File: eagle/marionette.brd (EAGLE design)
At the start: 112.4 x 152.7 mm, 47 parts, among them J2 SWD_CONNECTOR, J3 2X10FE, J4 2X10FE, J5 2X10FE, J6 2X10FE, J7 2X10FE, U1 USB3318, U2 NCP705, U3 XCL206B, X1 ABS25-32.768KHZ-6-T

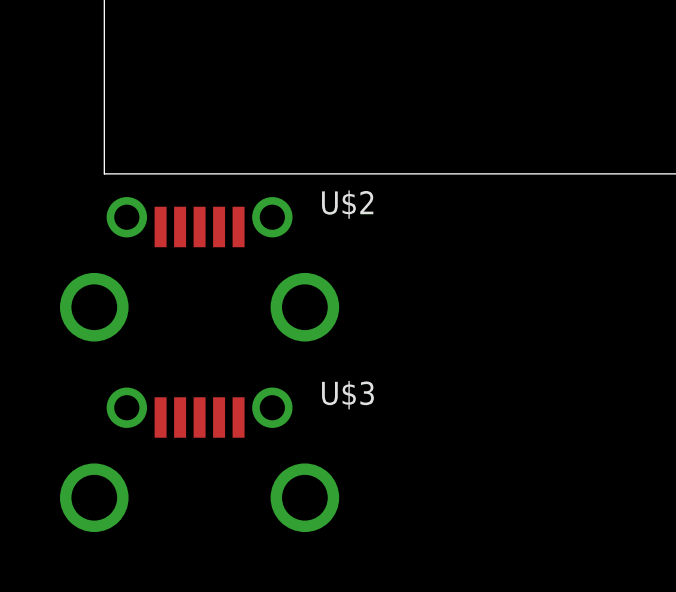
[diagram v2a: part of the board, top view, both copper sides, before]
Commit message: Replaced resistors and capacitors with Marionette library components
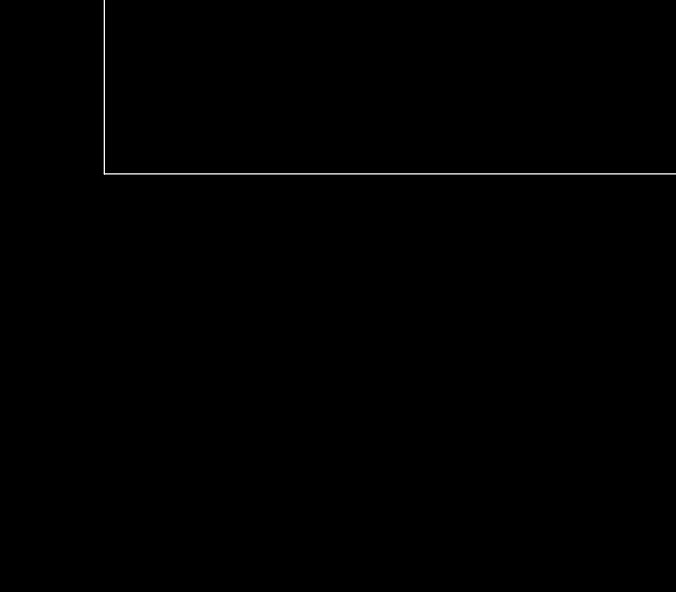
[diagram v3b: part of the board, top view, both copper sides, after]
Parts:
- removed U$2, U$3: ZX62D-B-5P8, con-hirose-microusb:ZX62D-B-5P8
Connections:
- removed net FS_DM: U$1.122, U$2.P2
- removed net FS_DP: U$1.123, U$2.P3
- removed net FS_ID: U$1.121, U$2.P4
- removed net OTG_VBUS: D2.P$1, U$1.120, U$2.P1
- removed net SHLD: U$3.P$1, U$3.P$2, U$3.P$3, U$3.P$4
- removed net VCC: U$3.P1
- new net N$13: U$1.122
- new net N$14: U$1.123
- new net N$2: U$1.120
- new net N$6: U$1.121
- net GND: no longer U$2.P$1, U$2.P$2, U$2.P$3, U$2.P$4, U$2.P5
- net N$12: no longer U$3.P5
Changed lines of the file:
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@@
 <layer number="54" name="bGND_GNDA" color="1" fill="9" visible="no" active="no"/>
 <layer number="56" name="wert" color="7" fill="1" visible="no" active="no"/>
-<layer number="59" name="Invisible" color="7" fill="1" visible="yes" active="yes"/>
-<layer number="61" name="stand" color="7" fill="1" visible="yes" active="yes"/>
 <layer number="90" name="Modules" color="5" fill="1" visible="no" active="no"/>
 <layer number="91" name="Nets" color="2" fill="1" visible="no" active="no"/>
@@
 <layer number="107" name="Crop" color="7" fill="1" visible="no" active="yes"/>
 <layer number="108" name="dxf_notes" color="14" fill="1" visible="yes" active="yes"/>
-<layer number="109" name="fp9" color="7" fill="1" visible="yes" active="yes"/>
 <layer number="110" name="labels" color="7" fill="1" visible="yes" active="yes"/>
 <layer number="111" name="print" color="7" fill="1" visible="yes" active="yes"/>
@@
 <layer number="121" name="_tsilk" color="7" fill="1" visible="no" active="yes"/>
 <layer number="122" name="_bsilk" color="7" fill="1" visible="no" active="yes"/>
-<layer number="123" name="tTestmark" color="7" fill="1" visible="yes" active="yes"/>
-<layer number="124" name="bTestmark" color="7" fill="1" visible="yes" active="yes"/>
 <layer number="125" name="_tNames" color="7" fill="1" visible="no" active="yes"/>
-<layer number="126" name="_bNames" color="7" fill="1" visible="yes" active="yes"/>
-<layer number="127" name="_tValues" color="7" fill="1" visible="yes" active="yes"/>
-<layer number="128" name="_bValues" color="7" fill="1" visible="yes" active="yes"/>
-<layer number="130" name="bLogo" color="7" fill="1" visible="yes" active="yes"/>
-<layer number="131" name="tText" color="7" fill="1" visible="yes" active="yes"/>
-<layer number="132" name="bMask" color="7" fill="1" visible="yes" active="yes"/>
 <layer number="144" name="Drill_legend" color="7" fill="1" visible="no" active="yes"/>
 <layer number="151" name="HeatSink" color="7" fill="1" visible="no" active="yes"/>
-<layer number="152" name="_bDocu" color="7" fill="1" visible="yes" active="yes"/>
-<layer number="199" name="Contour" color="7" fill="1" visible="yes" active="yes"/>
 <layer number="200" name="200bmp" color="1" fill="10" visible="no" active="yes"/>
 <layer number="201" name="201bmp" color="2" fill="10" visible="no" active="yes"/>
@@
 <layer number="223" name="223bmp" color="24" fill="1" visible="no" active="no"/>
 <layer number="224" name="224bmp" color="25" fill="1" visible="no" active="no"/>
-<layer number="225" name="225bmp" color="7" fill="1" visible="yes" active="yes"/>
-<layer number="226" name="226bmp" color="7" fill="1" visible="yes" active="yes"/>
-<layer number="227" name="227bmp" color="7" fill="1" visible="yes" active="yes"/>
-<layer number="228" name="228bmp" color="7" fill="1" visible="yes" active="yes"/>
-<layer number="231" name="Eagle3D_PG1" color="7" fill="1" visible="yes" active="yes"/>
-<layer number="232" name="Eagle3D_PG2" color="7" fill="1" visible="yes" active="yes"/>
-<layer number="233" name="Eagle3D_PG3" color="7" fill="1" visible="yes" active="yes"/>
-<layer number="248" name="Housing" color="7" fill="1" visible="yes" active="yes"/>
-<layer number="249" name="Edge" color="7" fill="1" visible="yes" active="yes"/>
 <layer number="250" name="Descript" color="3" fill="1" visible="no" active="no"/>
 <layer number="251" name="SMDround" color="12" fill="11" visible="no" active="no"/>
@@
 <element name="J6" library="20POS_ANGLED_FEMALE_HEADER" package="2X10_FEMALE_ANGLED" value="2X10FE" x="76.2" y="14.605"/>
 <element name="J7" library="20POS_ANGLED_FEMALE_HEADER" package="2X10_FEMALE_ANGLED" value="2X10FE" x="41.91" y="14.605"/>
-<element name="U$2" library="con-hirose-microusb" package="ZX62D-B-5P8" value="ZX62D-B-5P8" x="3.175" y="-4.445"/>
-<element name="U$3" library="con-hirose-microusb" package="ZX62D-B-5P8" value="ZX62D-B-5P8" x="3.175" y="-10.795"/>
 </elements>
 <signals>
@@
 <contactref element="C28" pad="2"/>
 <contactref element="C29" pad="2"/>
-<contactref element="U$3" pad="P5"/>
 <wire x1="35.56" y1="35.14" x2="38.1" y2="35.14" width="0" layer="19" extent="1-1"/>
 <wire x1="33.02" y1="35.14" x2="35.56" y2="35.14" width="0" layer="19" extent="1-1"/>
 <wire x1="36.83" y1="29.21" x2="38.1" y2="35.14" width="0" layer="19" extent="1-1"/>
-<wire x1="4.475" y1="-8.12" x2="36.83" y2="29.21" width="0" layer="19" extent="1-1"/>
 </signal>
 <signal name="N$7">
@@
 <contactref element="J4" pad="20"/>
 <contactref element="J3" pad="20"/>
-<contactref element="U$2" pad="P5"/>
-<contactref element="U$2" pad="P$1"/>
-<contactref element="U$2" pad="P$2"/>
-<contactref element="U$2" pad="P$3"/>
-<contactref element="U$2" pad="P$4"/>
 <wire x1="101.6" y1="64.135" x2="101.6" y2="95.885" width="0" layer="19" extent="1-1"/>
 <wire x1="78.955" y1="60.96" x2="101.6" y2="64.135" width="0" layer="19" extent="1-1"/>
@@
 <wire x1="101.6" y1="33.02" x2="78.955" y2="43.815" width="0" layer="19" extent="1-1"/>
 <wire x1="87.63" y1="13.335" x2="101.6" y2="33.02" width="0" layer="19" extent="1-1"/>
-<wire x1="5.6" y1="-1.445" x2="19.9" y2="44.45" width="0" layer="19" extent="1-1"/>
-<wire x1="4.475" y1="-1.77" x2="5.6" y2="-1.445" width="0" layer="19" extent="1-1"/>
-<wire x1="6.685" y1="-4.445" x2="5.6" y2="-1.445" width="0" layer="19" extent="1-1"/>
-<wire x1="0.75" y1="-1.445" x2="4.475" y2="-1.77" width="0" layer="19" extent="1-1"/>
-<wire x1="-0.335" y1="-4.445" x2="0.75" y2="-1.445" width="0" layer="19" extent="1-1"/>
 </signal>
 <signal name="SDIO_D4">
@@
 <contactref element="U$1" pad="58"/>
 </signal>
+<signal name="N$2">
+<contactref element="U$1" pad="120"/>
+</signal>
+<signal name="N$6">
+<contactref element="U$1" pad="121"/>
+</signal>
+<signal name="N$13">
+<contactref element="U$1" pad="122"/>
+</signal>
+<signal name="N$14">
+<contactref element="U$1" pad="123"/>
+</signal>
 <signal name="PA15">
 <contactref element="U$1" pad="138"/>
@@
 <wire x1="18.2" y1="44.45" x2="18.39" y2="46.065" width="0" layer="19" extent="1-1"/>
 </signal>
-<signal name="SHLD">
-<contactref element="U$3" pad="P$1"/>
-<contactref element="U$3" pad="P$2"/>
-<contactref element="U$3" pad="P$3"/>
-<contactref element="U$3" pad="P$4"/>
-<wire x1="0.75" y1="-7.795" x2="-0.335" y2="-10.795" width="0" layer="19" extent="1-1"/>
-<wire x1="5.6" y1="-7.795" x2="0.75" y2="-7.795" width="0" layer="19" extent="1-1"/>
-<wire x1="6.685" y1="-10.795" x2="5.6" y2="-7.795" width="0" layer="19" extent="1-1"/>
-</signal>
-<signal name="VCC">
-<contactref element="U$3" pad="P1"/>
-</signal>
-<signal name="OTG_VBUS">
-<contactref element="U$1" pad="120"/>
-<contactref element="U$2" pad="P1"/>
-<contactref element="D2" pad="P$1"/>
-<wire x1="13.12" y1="53.34" x2="73.71" y2="58.09" width="0" layer="19" extent="1-1"/>
-<wire x1="1.875" y1="-1.77" x2="13.12" y2="53.34" width="0" layer="19" extent="1-1"/>
-</signal>
-<signal name="FS_ID">
-<contactref element="U$1" pad="121"/>
-<contactref element="U$2" pad="P4"/>
-<wire x1="3.825" y1="-1.77" x2="73.71" y2="58.59" width="0" layer="19" extent="1-1"/>
-</signal>
-<signal name="FS_DM">
-<contactref element="U$1" pad="122"/>
-<contactref element="U$2" pad="P2"/>
-<wire x1="2.525" y1="-1.77" x2="73.71" y2="59.09" width="0" layer="19" extent="1-1"/>
-</signal>
-<signal name="FS_DP">
-<contactref element="U$1" pad="123"/>
-<contactref element="U$2" pad="P3"/>
-<wire x1="3.175" y1="-1.77" x2="73.71" y2="59.59" width="0" layer="19" extent="1-1"/>
-</signal>
 </signals>

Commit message: Added connections to the EDGE CONNECTOR OF DEATH!!!!!!!!!!!!!
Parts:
- added C31: 100nF, 10V, rcl_custom:.0603-C
- added R10, R11, R2, R3, R4, R5, R6, R7, R8, R9: 4.7k, rcl_custom:.0603-C
- added U$13: CON_HIROSE_DM3D(MICROSD), con-microsd-hirose-dm3:HIROSE_DM3D(MICRO-SD)
- added U$15: PTS645, PTS645:SMT
- added U$2, U$3: ZX62D-B-5P8, con-hirose-microusb:ZX62D-B-5P8
- C1, C10, C11, C12, C13, C14, C15, C16, C17, C18, C19, C2, C20, C21, C22, C23, C24, C25, C26, C28, C29, C3, C4, C5, C6, C7, C8, C9: device CAPACITOR_SMT:C0603 -> rcl_custom:.0603-C
- C27, C30: device CAPACITOR_SMT:C0402 -> rcl_custom:.0402-C
- R1: device RESISTOR:R0603 -> rcl_custom:.0603-C
- moved J2 73.9 mm to (1.92, 33.5), turned to 90 degrees
- moved J3 70.6 mm to (81.3, 16.5)
- moved J5 61.0 mm to (81.3, 79.5)
- moved U1 55.8 mm to (26.8, 84.1), turned to 270 degrees
- moved R1 50.9 mm to (30.6, 84.9), turned to 270 degrees
- moved C29 50.5 mm to (33.9, 84.6)
- moved C28 45.1 mm to (27.1, 79.0), turned to 180 degrees
- moved C18 43.2 mm to (34.6, 61.6)
- moved C20 40.8 mm to (34.2, 50.4)
- moved C21 36.7 mm to (34.2, 48.9)
- moved C6 36.0 mm to (43.2, 69.7)
- moved C17 31.9 mm to (49.4, 68.6)
- moved C24 31.8 mm to (62.4, 69.0), turned to 90 degrees
- moved C15 31.2 mm to (60.0, 69.2), turned to 90 degrees
- moved C16 30.4 mm to (54.4, 68.6)
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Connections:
- new net CAN1_RX: J5.2, U$1.11
- new net CAN1_TX: J5.1, U$1.128
- new net DAC1: J4.20, U$1.50
- new net FS_DM: U$1.122, U$2.P2
- new net FS_DP: U$1.123, U$2.P3
- new net FS_ID: U$1.121, U$2.P4
- new net I2C1_SCL: R6.1, U$1.164
- new net I2C1_SDA: R7.1, U$1.165
- new net I2C2_SLC: J3.19
- new net I2C2_SMBA: J3.20, U$1.18
- new net I2C3_SCL: J6.2, R4.1, U$1.84
- new net I2C3_SDA: J6.1, R5.1, U$1.85
- new net N$10: U$3.P3, U1.6
- new net N$11: U$3.P4, U1.1
- new net OTG_VBUS: D2.P$1, U$1.120, U$2.P1
- new net PE0: J4.9, U$1.169
- new net PE1: J4.10, U$1.170
- new net PE10: J4.19, U$1.73
- new net PE11: J5.3, U$1.74
- new net PE12: J5.4, U$1.75
- new net PE13: J5.5, U$1.76
- new net PE14: J5.6, U$1.77
- new net PE15: J5.7, U$1.78
- new net PE2: J4.11, U$1.1
- new net PE3: J4.12, U$1.2
- new net PE4: J4.13, U$1.3
- new net PE5: J4.14, U$1.4
- new net PE6: J4.15, U$1.5
- new net PE7: J4.16, U$1.68
- new net PE8: J4.17, U$1.69
- new net PE9: J4.18, U$1.70
- new net PF11: J5.8, U$1.59
- new net PF12: J5.9, U$1.60
- new net PF13: J5.10, U$1.63
- new net PF14: J5.11, U$1.64
- new net PF15: J5.12, U$1.65
- new net PG0: J5.13, U$1.66
- new net PG1: J5.14, U$1.67
- new net PG10: J6.6, U$1.153
- new net PG11: J6.7, U$1.154
- new net PG12: J6.8, U$1.155
- new net PG13: J6.9, U$1.156
- new net PG14: J6.10, U$1.157
- new net PG15: J6.11, U$1.160
- new net PG2: J5.15, U$1.106
- new net PG3: J5.16, U$1.107
- new net PG4: J5.17, U$1.108
- new net PG5: J5.18, U$1.109
- new net PG6: J5.19, U$1.110
- new net PG7: J5.20, U$1.111
- new net PG8: J6.4, U$1.112
- new net PG9: J6.5, U$1.152
- new net UART4_RX: J4.2, U$1.41
- new net UART4_TX: J4.1, U$1.40
- net +3.3VDD: now also R10.2, R11.2, R2.2, R3.2, R4.2, R5.2, R6.2, R7.2, R8.2, R9.2, U$13.P4, U1.17
- net +3.3VDDA: no longer C23.1, C24.1, U$1.38
- net ADC1/2/3_IN11: now also J7.4
- net ADC1/2/3_IN13: now also J7.5
- net ADC1/2/3_IN2: now also J7.1
- net ADC1/2_IN14: now also J7.6
- net ADC1/2_IN15: now also J7.7
- net ADC1/2_IN6: now also J7.2
- net ADC1/2_IN7: now also J7.3
- net ADC3_IN14: now also J7.9
- net ADC3_IN15: now also J7.10
- net ADC3_IN4: now also J7.11
- net ADC3_IN5: now also J7.12
- net ADC3_IN6: now also J7.13
- net ADC3_IN7: now also J7.14
- net ADC3_IN8: now also J7.15, J7.8
- net GND: now also C29.2, C31.2, U$13.G1, U$13.G2, U$13.G3, U$13.G4, U$13.P6, U$15.1, U$15.2, U$2.P$1, U$2.P$2, U$2.P$3, U$2.P$4, U$2.P5, U$3.P$1, U$3.P$2, U$3.P$3, U$3.P$4, U$3.P5; no longer J3.20, J4.20, J5.20, J6.20, J7.20
- net I2C2_SCL: now also R3.1
- net I2C2_SDA: now also J3.18, R2.1
- net I2C3_SMBA: now also J6.3, U$1.86; no longer U$1.18
- net N$12: no longer C29.2
- net N$13: now also C31.1, U$1.31, U$15.3, U$15.4; no longer U$1.122
- net N$14: now also C23.1, C24.1, U$1.38; no longer U$1.123
- net N$2: now also U$3.P1, U1.2; no longer U$1.120
- net N$6: now also U$3.P2, U1.5; no longer U$1.121
- net PA15: now also J3.5
- net PB14: now also J3.7
- net PB4: now also J3.6
- net PC15: now also J3.8
- net PD0: now also J3.9
- net PD1: now also J3.10
- net PD10: now also J4.3
- net PD11: now also J4.4
- net PD12: now also J4.5
- net PD13: now also J4.6
- net PD14: now also J4.7
- net PD15: now also J4.8
- net PD3: now also J3.11
- net PD4: now also J3.12
- net PD5: now also J3.13
- net PD6: now also J3.14
- net PD7: now also J3.15
- net PD8: now also J3.16
- net PD9: now also J3.17
- net PH10: now also J6.16
- net PH11: now also J6.17
- net PH12: now also J6.18
- net PH14: now also J6.19
- net PH15: now also J6.20
- net PH2: now also J6.12
- net PH3: now also J6.13
- net PH5: now also J6.14
- net PH6: now also J6.15
- net PI4: now also J7.16
- net PI5: now also J7.17
- net PI6: now also J7.18
- net PI7: now also J7.19
- net PI8: now also J7.20
- net SDIO_CK: now also U$13.P5
- net SDIO_CMD: now also U$13.P3
- net SDIO_D0: now also R8.1, U$13.P7
- net SDIO_D1: now also U$13.P8
- net SDIO_D2: now also R11.1, U$13.P1
- net SDIO_D3: now also R10.1, R9.1, U$13.P2
- net SPI2_MISO: now also J3.3
- net SPI2_MOSI: now also J3.4
- net SPI2_NSS: now also J3.1
- net SPI2_SCK: now also J3.2
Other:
- board size 112.4 x 152.7 mm -> 160.3 x 174 mm

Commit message: Updated board layout
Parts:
- moved J5 91.5 mm to (143.4, 12.3), turned to 0 degrees
- moved J4 47.0 mm to (111.3, 12.1), turned to 0 degrees
- moved J6 13.3 mm to (47.2, 11.8)
- moved J7 13.1 mm to (16.0, 11.8)
- moved J3 5.17 mm to (79.1, 11.8), turned to 0 degrees

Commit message: Added RGB led and resistors
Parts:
- added LED1: (no value), led-rgb-rohm:KINGBRITE_RGBLED_1.6X1.26
- added R12, R13, R14: (no value), rcl_custom:.0603-C
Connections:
- net SDIO_D7 renamed PC6
- removed net SDIO_D4: U$1.167
- removed net SDIO_D5: U$1.168
- removed net SDIO_D6: U$1.115
- new net B_LED: R14.1, U$1.115
- new net G_LED: R13.1, U$1.168
- new net N$16: LED1.3, R12.2
- new net N$17: LED1.4, R13.2
- new net N$18: LED1.1, R14.2
- new net R_LED: R12.1, U$1.167
- net +3.3VDD: now also LED1.2
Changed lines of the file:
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@@
 <attribute name="PB6" value="I2C1_SCL" x="50.8" y="52.07" size="1.778" layer="27" rot="R90" display="off"/>
 <attribute name="PB7" value="I2C1_SDA" x="50.8" y="52.07" size="1.778" layer="27" rot="R90" display="off"/>
-<attribute name="PB8" value="SDIO_D4" x="50.8" y="52.07" size="1.778" layer="27" rot="R90" display="off"/>
-<attribute name="PB9" value="SDIO_D5" x="50.8" y="52.07" size="1.778" layer="27" rot="R90" display="off"/>
+<attribute name="PB8" value="GPIO" x="50.8" y="52.07" size="1.778" layer="27" rot="R90" display="off"/>
+<attribute name="PB9" value="GPIO" x="50.8" y="52.07" size="1.778" layer="27" rot="R90" display="off"/>
 <attribute name="PH13" value="CAN1_TX" x="50.8" y="52.07" size="1.778" layer="27" rot="R90" display="off"/>
 <attribute name="PB10" value="UPLI_D3" x="50.8" y="52.07" size="1.778" layer="27" rot="R90" display="off"/>
@@
 <attribute name="PC4" value="ADC1/2_IN14" x="50.8" y="52.07" size="1.778" layer="27" rot="R90" display="off"/>
 <attribute name="PC5" value="ADC1/2_IN15" x="50.8" y="52.07" size="1.778" layer="27" rot="R90" display="off"/>
-<attribute name="PC6" value="SDIO_D6" x="50.8" y="52.07" size="1.778" layer="27" rot="R90" display="off"/>
-<attribute name="PC7" value="SDIO_D7" x="50.8" y="52.07" size="1.778" layer="27" rot="R90" display="off"/>
+<attribute name="PC6" value="GPIO" x="50.8" y="52.07" size="1.778" layer="27" rot="R90" display="off"/>
+<attribute name="PC7" value="GPIO" x="50.8" y="52.07" size="1.778" layer="27" rot="R90" display="off"/>
 <attribute name="PC8" value="SDIO_D0" x="50.8" y="52.07" size="1.778" layer="27" rot="R90" display="off"/>
 <attribute name="PA10" value="OTG_FS_ID" x="50.8" y="52.07" size="1.778" layer="27" rot="R90" display="off"/>
@@
 <element name="U3" library="XCL206B" package="56-BCPGA" value="XCL206B" x="21.07" y="48.91" rot="R270"/>
 <element name="X1" library="ABS25" package="4-SOJ" value="ABS25-32.768KHZ-6-T" x="44.04" y="33.56" rot="R270"/>
+<element name="LED1" library="led-rgb-rohm" package="KINGBRITE_RGBLED_1.6X1.26" value="" x="0.6" y="-1"/>
+<element name="R12" library="rcl_custom" package=".0603-C" value="" x="0.6" y="-3.9"/>
+<element name="R13" library="rcl_custom" package=".0603-C" value="" x="0.6" y="-6.8"/>
+<element name="R14" library="rcl_custom" package=".0603-C" value="" x="0.6" y="-9.7"/>
 </elements>
 <signals>
@@
 <wire x1="8.57" y1="81.89" x2="4.47" y2="66.355" width="0" layer="19" extent="1-1"/>
 </signal>
-<signal name="SDIO_D4">
-<contactref element="U$1" pad="167"/>
-</signal>
 <signal name="SDIO_CMD">
 <contactref element="U$1" pad="144"/>
@@
 <wire x1="42.53" y1="67.13" x2="39.372" y2="87.63" width="0" layer="19" extent="1-1"/>
 <wire x1="47.55" y1="64.82" x2="42.53" y2="67.13" width="0" layer="19" extent="1-1"/>
-</signal>
-<signal name="SDIO_D7">
-<contactref element="U$1" pad="116"/>
-</signal>
-<signal name="SDIO_D6">
-<contactref element="U$1" pad="115"/>
-</signal>
-<signal name="SDIO_D5">
-<contactref element="U$1" pad="168"/>
 </signal>
 <signal name="+3.3VDD">
@@
 <contactref element="U$1" pad="15"/>
 <contactref element="C22" pad="1"/>
+<contactref element="LED1" pad="2"/>
 <wire x1="68.97" y1="60.07" x2="68.96" y2="61.37" width="0" layer="19" extent="1-1"/>
 <wire x1="67.46" y1="63.03" x2="68.96" y2="61.37" width="0" layer="19" extent="1-1"/>
@@
 <wire x1="7.17" y1="81.89" x2="26.53" y2="85.85" width="0" layer="19" extent="1-1"/>
 <wire x1="2.555" y1="30.96" x2="20.132" y2="48.36" width="0" layer="19" extent="1-1"/>
+<wire x1="-0.2" y1="-1.55" x2="2.555" y2="30.96" width="0" layer="19" extent="1-1"/>
 </signal>
 <signal name="ADC1/2/3_IN2">
@@
 <contactref element="J3" pad="19"/>
 </signal>
+<signal name="N$16">
+<contactref element="LED1" pad="3"/>
+<contactref element="R12" pad="2"/>
+<wire x1="-0.2" y1="-0.45" x2="1.3" y2="-3.9" width="0" layer="19" extent="1-1"/>
+</signal>
+<signal name="N$17">
+<contactref element="LED1" pad="4"/>
+<contactref element="R13" pad="2"/>
+<wire x1="1.4" y1="-0.45" x2="1.3" y2="-6.8" width="0" layer="19" extent="1-1"/>
+</signal>
+<signal name="N$18">
+<contactref element="LED1" pad="1"/>
+<contactref element="R14" pad="2"/>
+<wire x1="1.4" y1="-1.55" x2="1.3" y2="-9.7" width="0" layer="19" extent="1-1"/>
+</signal>
+<signal name="R_LED">
+<contactref element="R12" pad="1"/>
+<contactref element="U$1" pad="167"/>
+<wire x1="-0.1" y1="-3.9" x2="38.05" y2="45.82" width="0" layer="19" extent="1-1"/>
+</signal>
+<signal name="G_LED">
+<contactref element="R13" pad="1"/>
+<contactref element="U$1" pad="168"/>
+<wire x1="-0.1" y1="-6.8" x2="38.05" y2="45.32" width="0" layer="19" extent="1-1"/>
+</signal>
+<signal name="B_LED">
+<contactref element="U$1" pad="115"/>
+<contactref element="R14" pad="1"/>
+<wire x1="-0.1" y1="-9.7" x2="48.55" y2="64.82" width="0" layer="19" extent="1-1"/>
+</signal>
+<signal name="PC6">
+<contactref element="U$1" pad="116"/>
+</signal>
 </signals>
